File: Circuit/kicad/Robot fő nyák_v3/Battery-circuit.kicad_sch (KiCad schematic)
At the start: 0 parts

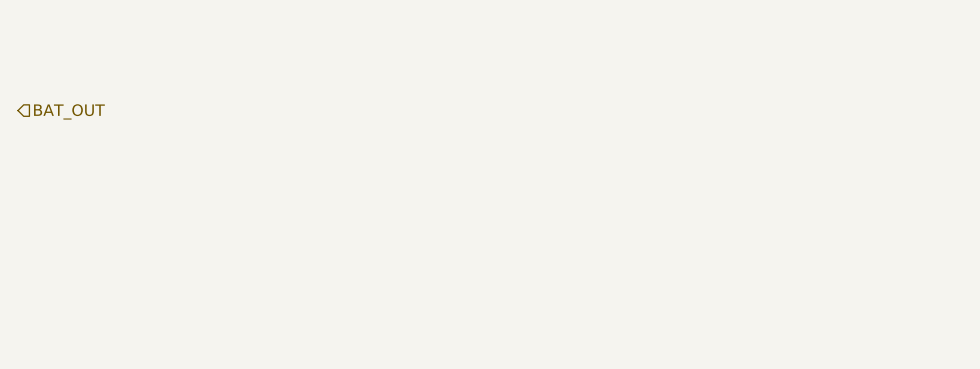
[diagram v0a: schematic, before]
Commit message: kicad  i2c and spi mux fixed and bugfixs
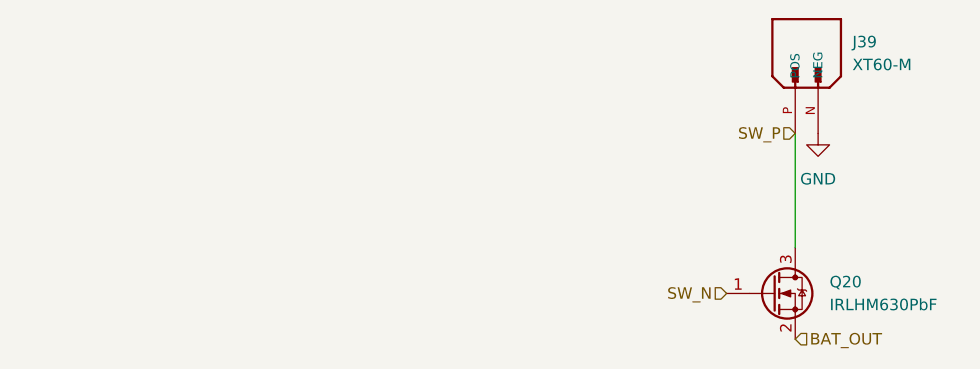
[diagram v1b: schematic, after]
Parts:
- added J39: XT60-M, XT60-M:AMASS_XT60-M, symbol xt-60:XT60-M
- added Q20: IRLHM630PbF, Package_TO_SOT_SMD:PQFN_8x8, symbol Transistor_FET:IRLML0030
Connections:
- net BAT_OUT: now also Q20.2 (S)
- new net GND: J39.N (NEG)
- new net SW_N: Q20.1 (G)
- new net SW_P: J39.P (POS), Q20.3 (D)

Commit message: readme updated kicad circuit V1
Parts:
- J1: renamed from J39; footprint XT60-M:AMASS_XT60-M -> Connector_AMASS:AMASS_XT60-M_1x02_P7.20mm_Vertical
- renumbered Q20 to Q26
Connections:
- net GND: now also J1.1 (NEG); no longer J1.N (NEG)
- net SW_P: now also J1.2 (POS); no longer J1.P (POS)
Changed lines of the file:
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@@
 		(dnp no)
 		(fields_autoplaced yes)
-		(property "Reference" "J39"
+		(property "Reference" "J1"
 			(at 198.12 57.1499 90)
 			(effects
@@
 			)
 		)
-		(property "Footprint" "XT60-M:AMASS_XT60-M"
-			(at 194.31 62.23 0)
+		(property "Footprint" "Connector_AMASS:AMASS_XT60-M_1x02_P7.20mm_Vertical"
+			(at 204.724 62.484 0)
 			(effects
 				(font
@@
 		)
 		(property "MF" "AMASS"
-			(at 194.31 62.23 0)
+			(at 204.724 61.976 0)
 			(effects
 				(font
@@
 		)
 		(property "MAXIMUM_PACKAGE_HEIGHT" "16.00 mm"
-			(at 194.31 62.23 0)
+			(at 204.724 61.976 0)
 			(effects
 				(font
@@
 		)
 		(property "Package" "Package"
-			(at 194.31 62.23 0)
+			(at 204.724 61.976 0)
 			(effects
 				(font
@@
 		)
 		(property "Price" "None"
-			(at 194.31 62.23 0)
+			(at 204.724 61.976 0)
 			(effects
 				(font
@@
 		)
 		(property "Check_prices" "https://www.snapeda.com/parts/XT60-M/AMASS/view-part/?ref=eda"
-			(at 194.31 62.23 0)
+			(at 204.724 62.484 0)
 			(effects
 				(font
@@
 		)
 		(property "STANDARD" "IPC 7351B"
-			(at 194.31 62.23 0)
+			(at 204.724 61.976 0)
 			(effects
 				(font
@@
 		)
 		(property "PARTREV" "V1.2"
-			(at 194.31 62.23 0)
+			(at 204.724 61.976 0)
 			(effects
 				(font
@@
 		)
 		(property "SnapEDA_Link" "https://www.snapeda.com/parts/XT60-M/AMASS/view-part/?ref=snap"
-			(at 194.31 62.23 0)
+			(at 204.724 62.484 0)
 			(effects
 				(font
@@
 		)
 		(property "MP" "XT60-M"
-			(at 194.31 62.23 0)
+			(at 204.724 61.976 0)
 			(effects
 				(font
@@
 		)
 		(property "Description_1" "Plug; DC supply; XT60; male; PIN: 2; for cable; soldered; 30A; 500V"
-			(at 194.31 62.23 0)
+			(at 204.724 62.484 0)
 			(effects
 				(font
@@
 		)
 		(property "Availability" "Not in stock"
-			(at 194.31 62.23 0)
+			(at 204.724 61.976 0)
 			(effects
 				(font
@@
 		)
 		(property "MANUFACTURER" "AMASS"
-			(at 194.31 62.23 0)
-			(effects
-				(font
-					(size 1.27 1.27)
-				)
-				(justify bottom)
-				(hide yes)
-			)
-		)
-		(pin "P"
-		)
-		(pin "N"
+			(at 204.724 61.976 0)
+			(effects
+				(font
+					(size 1.27 1.27)
+				)
+				(justify bottom)
+				(hide yes)
+			)
+		)
+		(pin "1"
+		)
+		(pin "2"
 		)
 		(instances
 			(project ""
 				(path "/e63e39d7-6ac0-4ffd-8aa3-1841a4541b55/22d35cae-4904-48d0-a6f6-5ba5919dfbde"
-					(reference "J39")
+					(reference "J1")
 					(unit 1)
 				)
@@
 		(dnp no)
 		(fields_autoplaced yes)
-		(property "Reference" "Q20"
+		(property "Reference" "Q26"
 			(at 195.58 83.8199 0)
 			(effects
@@
 			(project "CM5IO"
 				(path "/e63e39d7-6ac0-4ffd-8aa3-1841a4541b55/22d35cae-4904-48d0-a6f6-5ba5919dfbde"
-					(reference "Q20")
+					(reference "Q26")
 					(unit 1)
 				)
@@
 		(dnp no)
 		(fields_autoplaced yes)
-		(property "Reference" "#PWR0138"
+		(property "Reference" "#PWR0160"
 			(at 194.31 73.66 0)
 			(effects
@@
 			(project ""
 				(path "/e63e39d7-6ac0-4ffd-8aa3-1841a4541b55/22d35cae-4904-48d0-a6f6-5ba5919dfbde"
-					(reference "#PWR0138")
+					(reference "#PWR0160")
 					(unit 1)
 				)

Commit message: kicad update
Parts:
- added Q30: NMOS, symbol Simulation_SPICE:NMOS
- added R96: 500k, symbol Device:R
- added SW5: SW_SPST, symbol Switch:SW_SPST
- added U38: IP2721, Package_SO:TSSOP-16_4.4x5mm_P0.65mm, symbol Interface_USB:IP2721
- added U6: BQ24650, Package_DFN_QFN:Texas_RVA_VQFN-16-1EP_3.5x3.5mm_P0.5mm_EP2.14x2.14mm_ThermalVias, symbol Battery_Management:BQ24650
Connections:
- net GND: now also R96.2, U38.5 (GND)
- net SW_N: now also SW5.2 (B)
- net SW_P: now also R96.1, SW5.1 (A)
- new net: Q30.2 (G), U38.1 (VBUSG)
- new net: Q30.3 (S), U38.16 (VBUS)
- new net: U6.11 (GND), U6.17 (GND)
- new net PD-CHARGE_CC1: U38.12 (CC2)
- new net PD-CHARGE_CC2: U38.13 (CC1)
- new net PD-CHARGE_VBUS: Q30.1 (D), U38.11 (SEL), U38.2 (VIN)
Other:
- moved on the sheet: J1, Q26

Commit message: kicad update
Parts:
- removed Q26: IRLHM630PbF, Package_TO_SOT_SMD:PQFN_8x8, symbol Transistor_FET:IRLML0030
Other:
- note added: "a bq egy lehetséges megoldás, de nem egyszerű összeállítani"
- note added: "valahogy meg kéne oldani védelemnek a lekapcsolást, amely pl egy gomb hatására indul csak újra"
- moved on the sheet: U6
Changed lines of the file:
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@@
 	(generator_version "9.0")
 	(paper "A4")
-	(junction
-		(at 210.82 80.01)
-		(diameter 0)
-		(color 0 0 0 0)
+	(text "a bq egy lehetséges megoldás, de nem egyszerű összeállítani\n"
+		(exclude_from_sim no)
+		(at 138.684 92.456 0)
+		(effects
+			(font
+				(size 1.27 1.27)
+			)
+		)
+	)
+	(text "valahogy meg kéne oldani védelemnek a lekapcsolást, \namely pl egy gomb hatására indul csak újra"
+		(exclude_from_sim no)
+		(at 230.378 102.108 0)
+		(effects
+			(font
+				(size 1.27 1.27)
+			)
+		)
 	)
 	(junction
@@
 	(wire
 		(pts
-			(xy 210.82 80.01) (xy 210.82 90.17)
-		)
-		(stroke
-			(width 0)
-			(type default)
-		)
-	)
-	(wire
-		(pts
-			(xy 208.28 80.01) (xy 210.82 80.01)
+			(xy 208.28 80.01) (xy 214.63 80.01)
 		)
 		(stroke
@@
 		(pts
 			(xy 152.4 52.2478) (xy 173.99 52.2478)
-		)
-		(stroke
-			(width 0)
-			(type default)
-		)
-	)
-	(wire
-		(pts
-			(xy 210.82 80.01) (xy 214.63 80.01)
 		)
 		(stroke
@@
 				(hide yes)
 			)
-		)
-	)
-	(hierarchical_label "BAT_OUT"
-		(shape input)
-		(at 227.33 102.87 0)
-		(effects
-			(font
-				(size 1.27 1.27)
-			)
-			(justify left)
 		)
 	)
@@
 	(symbol
 		(lib_id "Battery_Management:BQ24650")
-		(at 88.9 129.54 0)
+		(at 127 121.92 0)
 		(unit 1)
 		(exclude_from_sim no)
@@
 		(fields_autoplaced yes)
 		(property "Reference" "U6"
-			(at 91.0433 104.14 0)
+			(at 129.1433 96.52 0)
 			(effects
 				(font
@@
 		)
 		(property "Value" "BQ24650"
-			(at 91.0433 106.68 0)
+			(at 129.1433 99.06 0)
 			(effects
 				(font
@@
 		)
 		(property "Footprint" "Package_DFN_QFN:Texas_RVA_VQFN-16-1EP_3.5x3.5mm_P0.5mm_EP2.14x2.14mm_ThermalVias"
-			(at 88.9 175.26 0)
+			(at 127 167.64 0)
 			(effects
 				(font
@@
 		)
 		(property "Datasheet" "https://www.ti.com/lit/ds/symlink/bq24650.pdf"
-			(at 88.9 134.62 0)
+			(at 127 127 0)
 			(effects
 				(font
@@
 		)
 		(property "Description" "10A, 28V max voltage, Battery Charger w/600kHz NMOS-NMOS Synchronous Buck Converter for Solar, VQFN-16"
-			(at 88.9 134.62 0)
+			(at 127 127 0)
 			(effects
 				(font
@@
 					(unit 1)
 				)
-			)
-		)
-	)
-	(symbol
-		(lib_id "Transistor_FET:IRLML0030")
-		(at 224.79 97.79 0)
-		(unit 1)
-		(exclude_from_sim no)
-		(in_bom yes)
-		(on_board yes)
-		(dnp no)
-		(fields_autoplaced yes)
-		(property "Reference" "Q26"
-			(at 231.14 96.5199 0)
-			(effects
-				(font
-					(size 1.27 1.27)
-				)
-				(justify left)
-			)
-		)
-		(property "Value" "IRLHM630PbF"
-			(at 231.14 99.0599 0)
-			(effects
-				(font
-					(size 1.27 1.27)
-				)
-				(justify left)
-			)
-		)
-		(property "Footprint" "Package_TO_SOT_SMD:PQFN_8x8"
-			(at 229.87 99.695 0)
-			(effects
-				(font
-					(size 1.27 1.27)
-					(italic yes)
-				)
-				(justify left)
-				(hide yes)
-			)
-		)
-		(property "Datasheet" "https://www.infineon.com/dgdl/irlml0030pbf.pdf?fileId=5546d462533600a401535664773825df"
-			(at 229.87 101.6 0)
-			(effects
-				(font
-					(size 1.27 1.27)
-				)
-				(justify left)
-				(hide yes)
-			)
-		)
-		(property "Description" "5.3A Id, 30V Vds, 27mOhm Rds, N-Channel HEXFET Power MOSFET, SOT-23"
-			(at 224.79 97.79 0)
-			(effects
-				(font
-					(size 1.27 1.27)
-				)
-				(hide yes)
-			)
-		)
-		(pin "3"
-		)
-		(pin "1"
-		)
-		(pin "2"
-		)
-		(instances
-			(project "CM5IO"
-				(path "/e63e39d7-6ac0-4ffd-8aa3-1841a4541b55/22d35cae-4904-48d0-a6f6-5ba5919dfbde"
-					(reference "Q26")
-					(unit 1)
-				)
